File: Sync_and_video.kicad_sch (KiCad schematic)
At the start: 37 parts, among them P1 500R, Q7 2N2907, U10 74LS13, U11 74LS10, U12 74LS393, U13 74LS00, U15 74LS20, U16 74LS04, U29 74LS00, U3 74LS10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

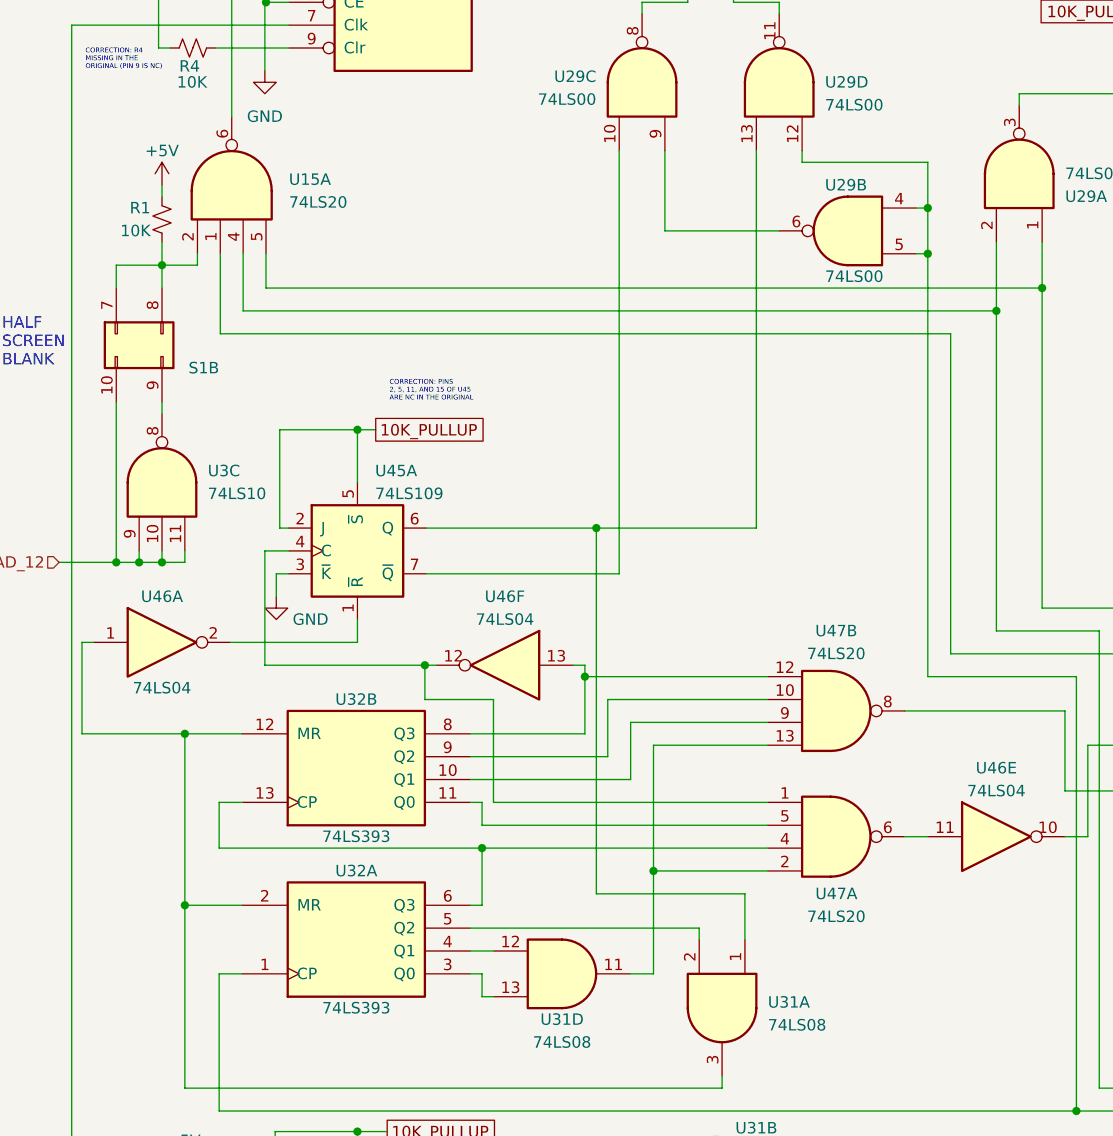
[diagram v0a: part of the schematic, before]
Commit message: Various corrections. Add new symbols and footprints
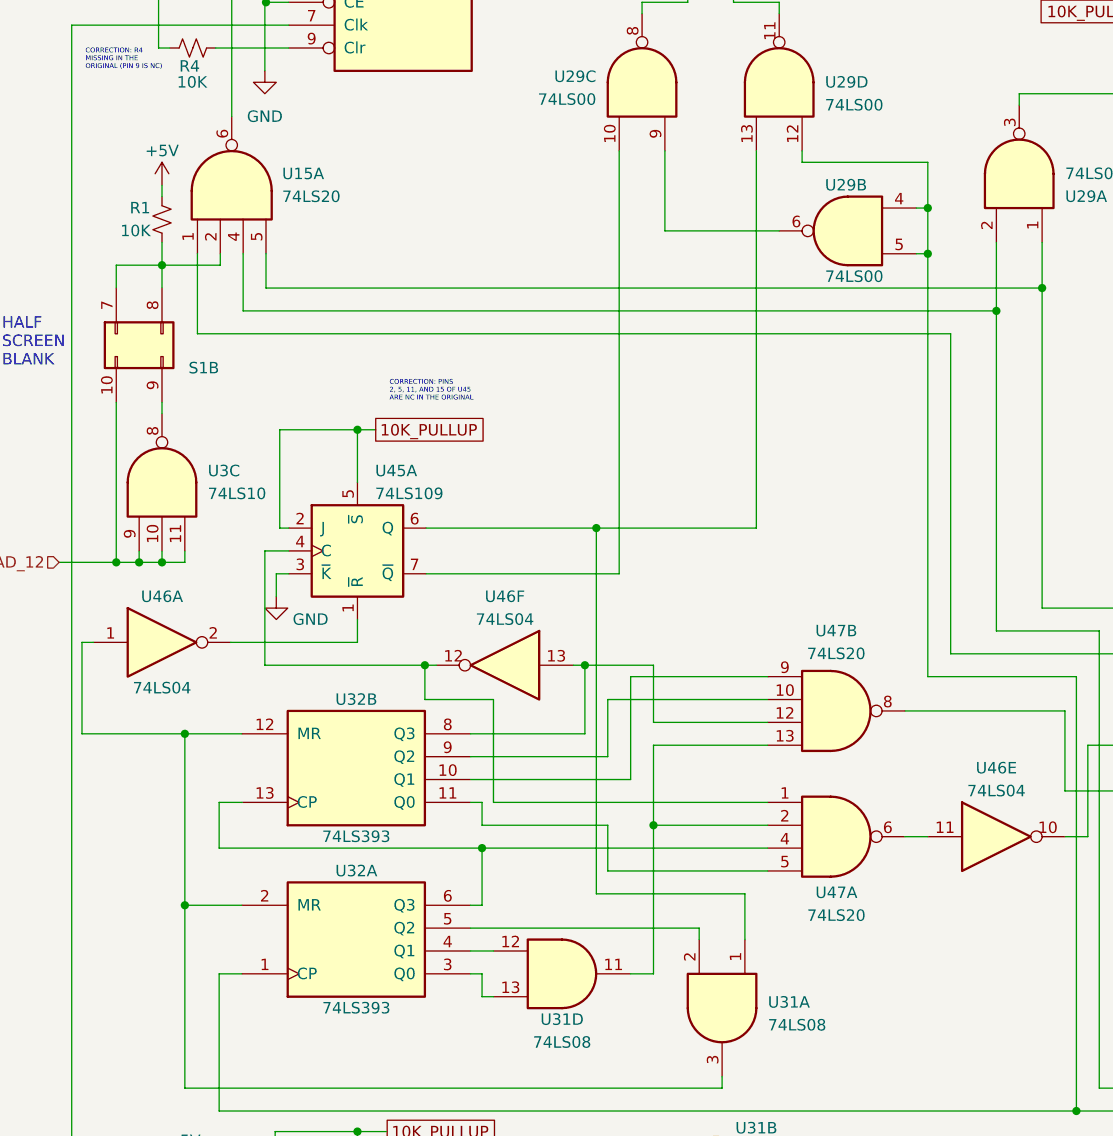
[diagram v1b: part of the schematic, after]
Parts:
- removed U15: 74LS20, symbol K-1008_Library:74LS20_U15
- removed U47: 74LS20, symbol K-1008_Library:74LS20_U47
- added U15, U47: 74LS20, symbol K-1008_Library:74LS20
- C11, C17, C33, C5: footprint (none) -> K-1008:C_Disc_D8.0mm_W2.5mm_P6.35mm
- P1: footprint (none) -> K-1008:Potentiometer_Bourns_3339P_Vertical_HandSoldering
- Q7: footprint Package_TO_SOT_THT:TO-92_Inline -> K-1008:TO-92
- R1, R10, R12, R13, R4: footprint (none) -> K-1008:R_Axial_DIN0309_10K_L6.3mm_D2.3mm_P12.70mm_Horizontal
- R14, R15: footprint (none) -> K-1008:R_Axial_DIN0309_68R_L6.3mm_D2.3mm_P12.70mm_Horizontal
- R16: footprint (none) -> K-1008:R_Axial_DIN0309_220R_L6.3mm_D2.3mm_P12.70mm_Horizontal
- R17, R18: footprint (none) -> K-1008:R_Axial_DIN0309_1K_L6.3mm_D2.3mm_P12.06mm_Horizontal
- R2, R5: footprint (none) -> K-1008:R_Axial_DIN0309_2K2_L6.3mm_D2.3mm_P12.70mm_Horizontal
- R3: footprint (none) -> K-1008:R_Axial_DIN0309_470R_L6.3mm_D2.3mm_P12.70mm_Horizontal
- S1, U30, U45, U8, U9: footprint (none) -> K-1008:DIP-16_W7.62mm_LongPads
- U10: footprint (none) -> K-1008:DIP-14_W7.62mm_LongPads; symbol 74xx:74LS13 -> K-1008_Library:74LS13
- U11, U12, U13, U16, U29, U3, U31, U32, U44, U46: footprint (none) -> K-1008:DIP-14_W7.62mm_LongPads
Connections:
- net HORIZ_UNBLK: now also U15.4
- net at U45.4 (C), U46.12: now also U47.1
- net at U31.11: now also U47.13, U47.2
- net at U32.13 (CP), U32.6 (Q3): now also U47.4
- net at U32.11 (Q0): now also U47.5
- net at U46.11: now also U47.6
- net at U45.10 (Q): now also U15.1
- net at R1.1, S1.7 (Pin_7), S1.8 (Pin_8): now also U15.2
- net at U16.6, U29.1: now also U15.5
- net at U9.15 (PE): now also U15.6
- net at U32.10 (Q1): now also U47.9
- net at U32.8 (Q3), U46.13: now also U47.12
- net at U32.9 (Q2): now also U47.10
- net at U45.13 (~{K}): now also U47.8

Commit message: Routing completed
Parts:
- added unit 4 of U10
- added unit 4 of U47
- U47: footprint (none) -> K-1008:DIP-14_W7.62mm_LongPads
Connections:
- net +5V: now also U45.3 (~{K})
- net DOT_CLK: now also P1.1; no longer P1.3
- net GND: now also U10.11 (N/C); no longer U45.3 (~{K})
- net at U31.11, U47.13, U47.2: now also U47.3 (N/C)
- net at C5.1, R2.1, R5.2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: now also U10.3 (N/C)
- net at R2.2: now also P1.3; no longer P1.1
- no-connect marks 3 -> 4
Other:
- note added: "CORRECTION: ~{K} IS CONNECTED TO GND IN THE ORIGINAL"
- moved on the sheet: P1

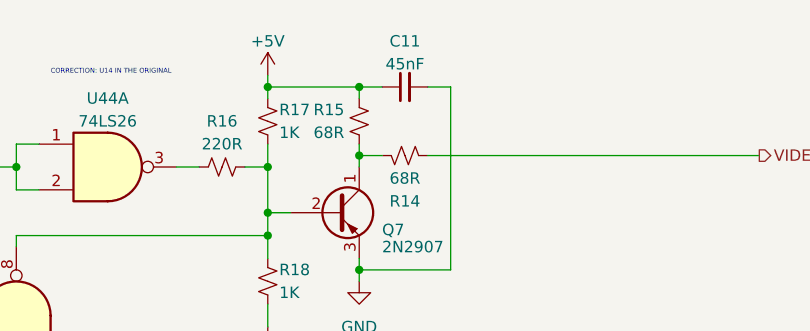
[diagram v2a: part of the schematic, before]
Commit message: Correct C45 value
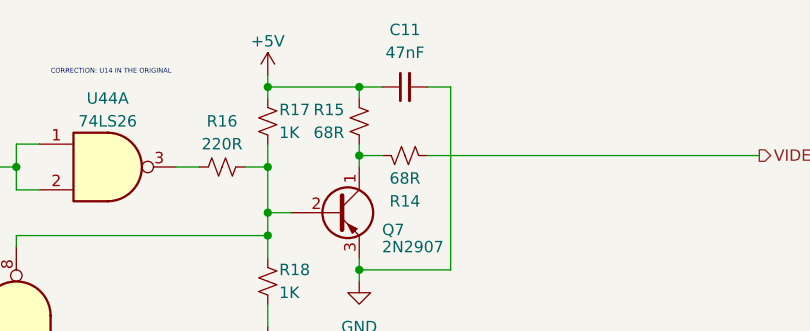
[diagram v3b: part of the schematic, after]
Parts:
- C11: value 45nF -> 47nF
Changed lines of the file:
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@@
   (symbol (lib_id "Device:C_Small") (at 141.605 22.86 90) (unit 1)
     (in_bom yes) (on_board yes) (dnp no) (fields_autoplaced)
-    (property "Reference" "C11" (at 141.6113 17.78 90)
+    (property "Reference" "C11" (at 141.6113 16.51 90)
       (effects (font (size 1.27 1.27)))
     )
-    (property "Value" "45nF" (at 141.6113 20.32 90)
+    (property "Value" "47nF" (at 141.6113 19.05 90)
       (effects (font (size 1.27 1.27)))
     )
